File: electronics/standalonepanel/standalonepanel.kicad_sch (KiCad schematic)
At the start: 95 parts, among them J1 LEDPWR, J2 USB_C-PD, J3 Speaker, J4 Conn_01x07_Pin, SW1 UP, SW2 BOOT, SW3 SET, SW4 DOWN, SW5 TST-ICE40, SW6 RESET, U1 SC189ZSKTRT, U10 DS3231, U11 SN74LVC8T245, U12 SN74LVC8T245, U13 SN74LVC8T245, U2 SC189CSKTRT, U3 CH340C, U4 ESP32-WROVER-E, U5 IS64WV25616EFBLL-10TLI, U6 MAX98357A, U7 ICE40-HX4K, X1 12MHz

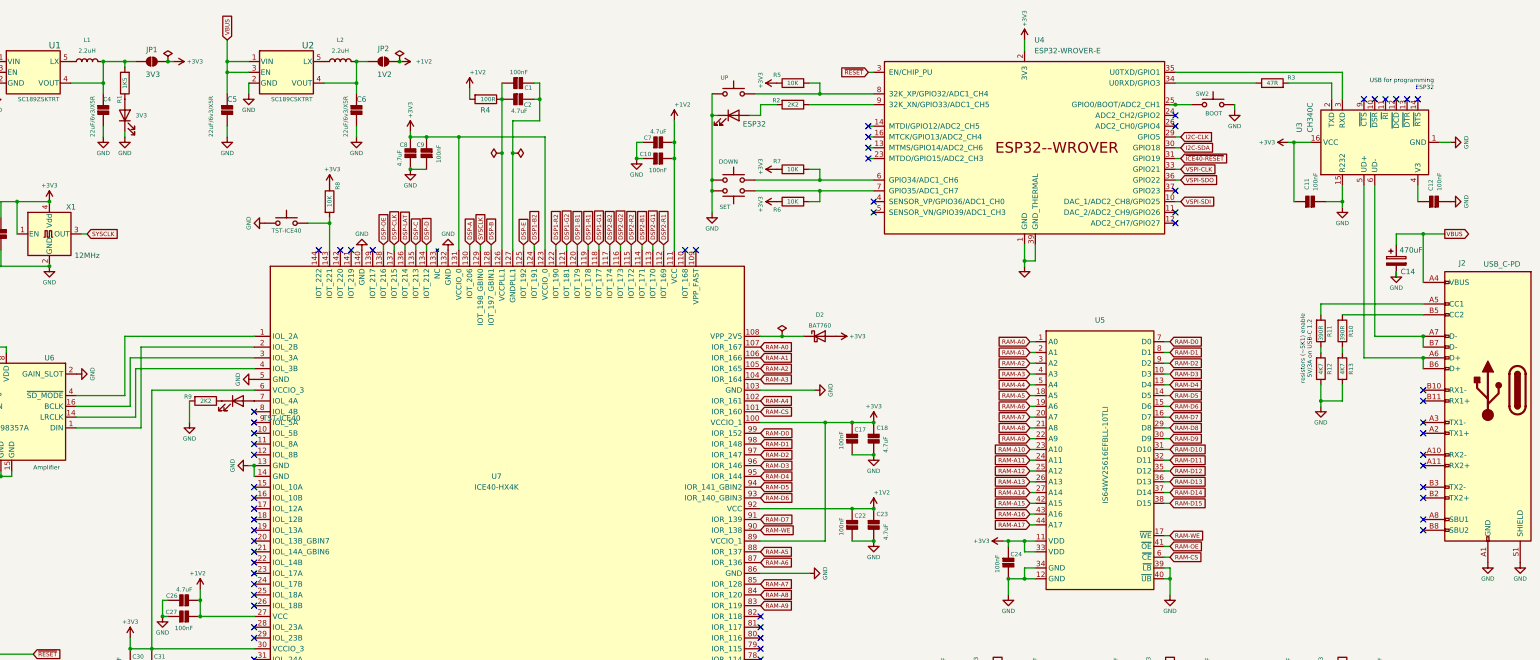
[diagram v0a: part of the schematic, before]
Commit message: cleanup kicad files and added overview documentation
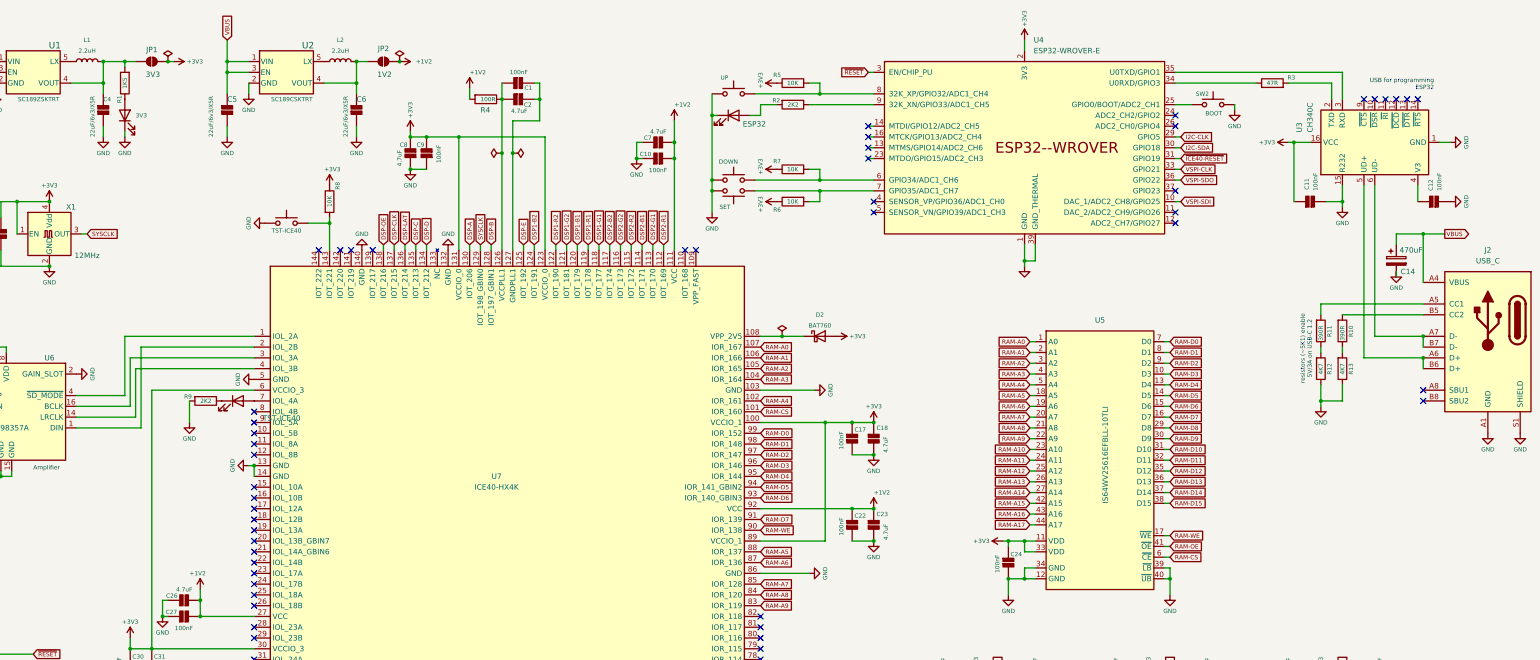
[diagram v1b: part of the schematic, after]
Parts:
- removed J2: USB_C-PD, 0_whitemagic:USB_C_Receptacle_G-Switch_GT-USB-7010ASV, symbol 0_project:USB_C-PD
- removed U4: ESP32-WROVER-E, 0_whitemagic:ESP32-WROVER-E, symbol 0_project:ESP32-WROVER-E
- added J2: USB_C, 0_whitemagic:USB_C_Receptacle _12pins, symbol 0_whitemagic:USB_C
- added U4: ESP32-WROVER-E, 0_whitemagic:ESP32-WROVER-E, symbol 0_whitemagic:ESP32-WROVER-E
- BT1: symbol 0_project:Battery_Cell -> 0_whitemagic:Battery_Cell
- C1, C10, C11, C12, C13, C17, C18, C2, C22, C23, C24, C26, C27, C28, C29, C3, C30, C31, C32, C33, C34, C35, C36, C37, C38, C39, C4, C40, C41, C42, C43, C44, C45, C46, C47, C5, C6, C7, C8, C9: symbol 0_project:C -> 0_whitemagic:C
- U1, U2: symbol 0_project:SC189ZSKTRT -> 0_whitemagic:SC189ZSKTRT
- U3: symbol 0_project:CH340C -> 0_whitemagic:CH340C
- U5: symbol 0_project:IS64WV25616EFBLL -> 0_whitemagic:IS64WV25616EFBLL
- U6: symbol 0_project:MAX98357A -> 0_whitemagic:MAX98357A
- U7: symbol 0_project:ICE40HX4K-TQ144 -> 0_whitemagic:ICE40HX4K-TQ144
- X1: symbol 0_project:TXC-7C -> 0_whitemagic:TXC-7C
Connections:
- net +3V3: now also U4.2 (3V3)
- net GND: now also J2.A1 (GND), J2.A12 (GND), J2.B1 (GND), J2.B12 (GND), J2.S1 (SHIELD), U4.1 (GND), U4.15 (GND), U4.38 (GND), U4.39 (GND_THERMAL)
- net I2C-CLK: now also U4.29 (GPIO5)
- net I2C-SDA: now also U4.30 (GPIO18)
- net VBUS: now also J2.A4 (VBUS), J2.A9 (VBUS), J2.B4 (VBUS), J2.B9 (VBUS)
- net VSPI-CLK: now also U4.33 (GPIO21)
- net VSPI-SDI: now also U4.10 (DAC_1/ADC2_CH8/GPIO25)
- net VSPI-SDO: now also U4.36 (GPIO22)
- net ~{ICE40-RESET}: now also U4.31 (GPIO19)
- net ~{RESET}: now also U4.3 (EN/CHIP_PU)
- net at SW2.1: now also U4.25 (GPIO0/BOOT/ADC2_CH1)
- net at R3.1: now also U4.34 (U0RXD/GPIO3)
- net at U3.3 (RXD): now also U4.35 (U0TXD/GPIO1)
- net at R7.2, SW4.2: now also U4.6 (GPIO34/ADC1_CH6)
- net at R6.2, SW3.2: now also U4.7 (GPIO35/ADC1_CH7)
- net at R5.2, SW1.2: now also U4.8 (32K_XP/GPIO32/ADC1_CH4)
- net at R2.1: now also U4.9 (32K_XN/GPIO33/ADC1_CH5)
- net at R11.2: now also J2.A5 (CC1)
- net at U3.5 (UD+): now also J2.A6 (D+), J2.B6 (D+)
- net at U3.6 (UD-): now also J2.A7 (D-), J2.B7 (D-)
- net at R10.2: now also J2.B5 (CC2)
- no-connect marks 78 -> 70
